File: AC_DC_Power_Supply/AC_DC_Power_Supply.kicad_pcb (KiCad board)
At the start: 2 copper layers, 6 parts, among them J1 Conn_01x02_Socket, J2 Conn_01x02_Socket, U1 L7805

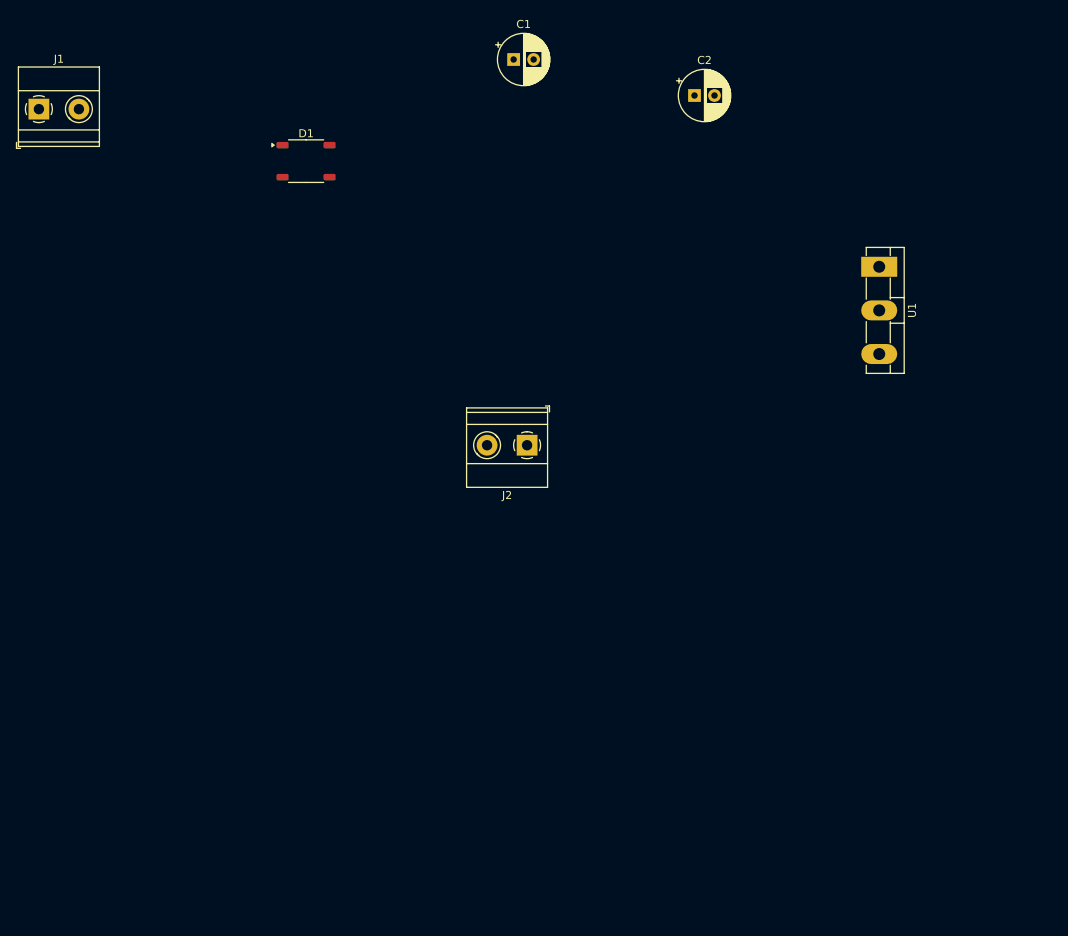
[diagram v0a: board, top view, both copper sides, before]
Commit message: power supply AC_DC
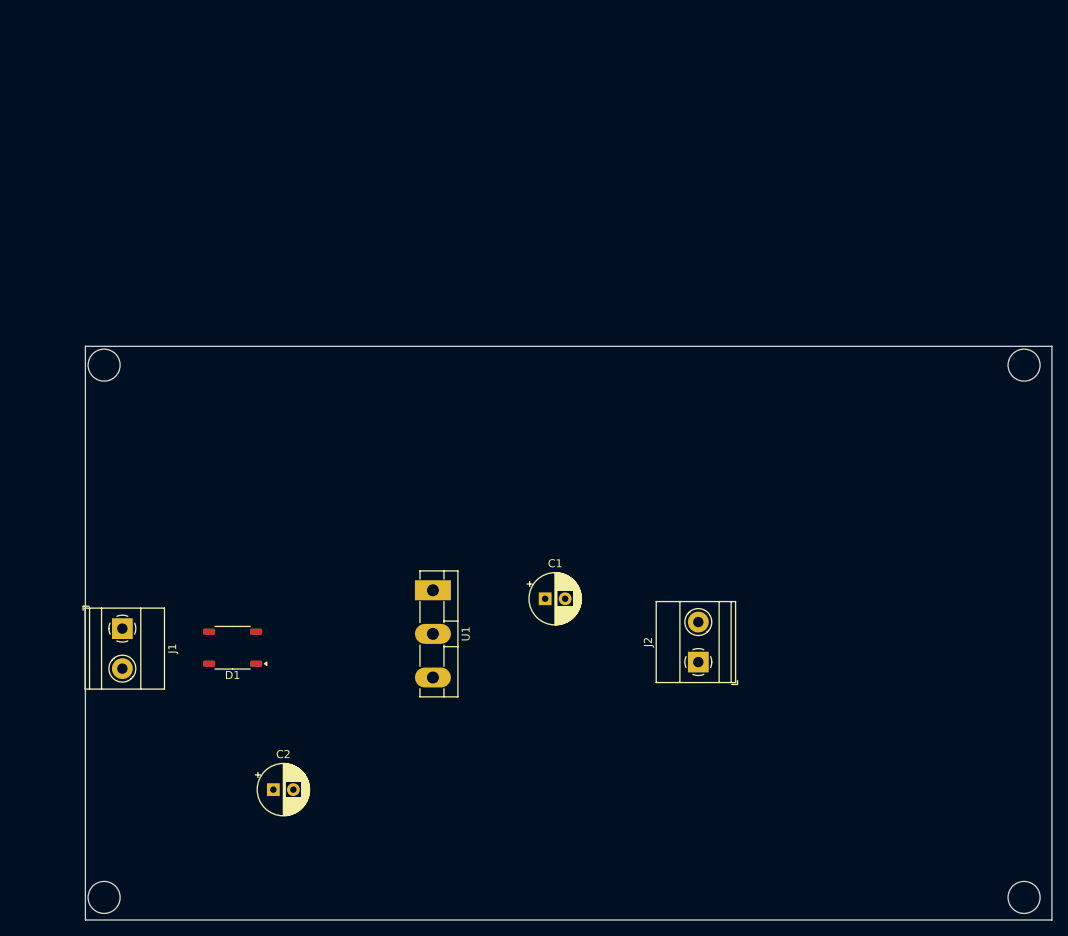
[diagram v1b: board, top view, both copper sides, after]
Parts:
- moved C2 101.4 mm to (96.7, 144.1)
- moved U1 68.9 mm to (116.6, 119.2)
- moved C1 67.5 mm to (130.7, 120.3)
- moved J1 65.7 mm to (77.8, 124.0), turned to -90 degrees
- moved D1 61.5 mm to (91.6, 126.4), turned to 180 degrees
- moved J2 34.5 mm to (149.8, 128.2), turned to 90 degrees
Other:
- board outline added: 120.8 x 71.7 mm
